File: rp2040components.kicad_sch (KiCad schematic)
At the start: 9 parts, among them J2 Conn_01x02, U8 W25Q128JVSIQTR, U9 ABM8-272-T3_C20625731

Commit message: Renamed page 2
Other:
- title: RP2040 basic -> RP2040 Components
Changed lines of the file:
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@@
 	(paper "A4")
 	(title_block
-		(title "RP2040 basic")
+		(title "RP2040 Components")
 	)
 	(text "Not sure if this is required. \nwe can optionally have a bootsel bridge \nhere. bridging QSPI_SS to GND\n-alister\n"

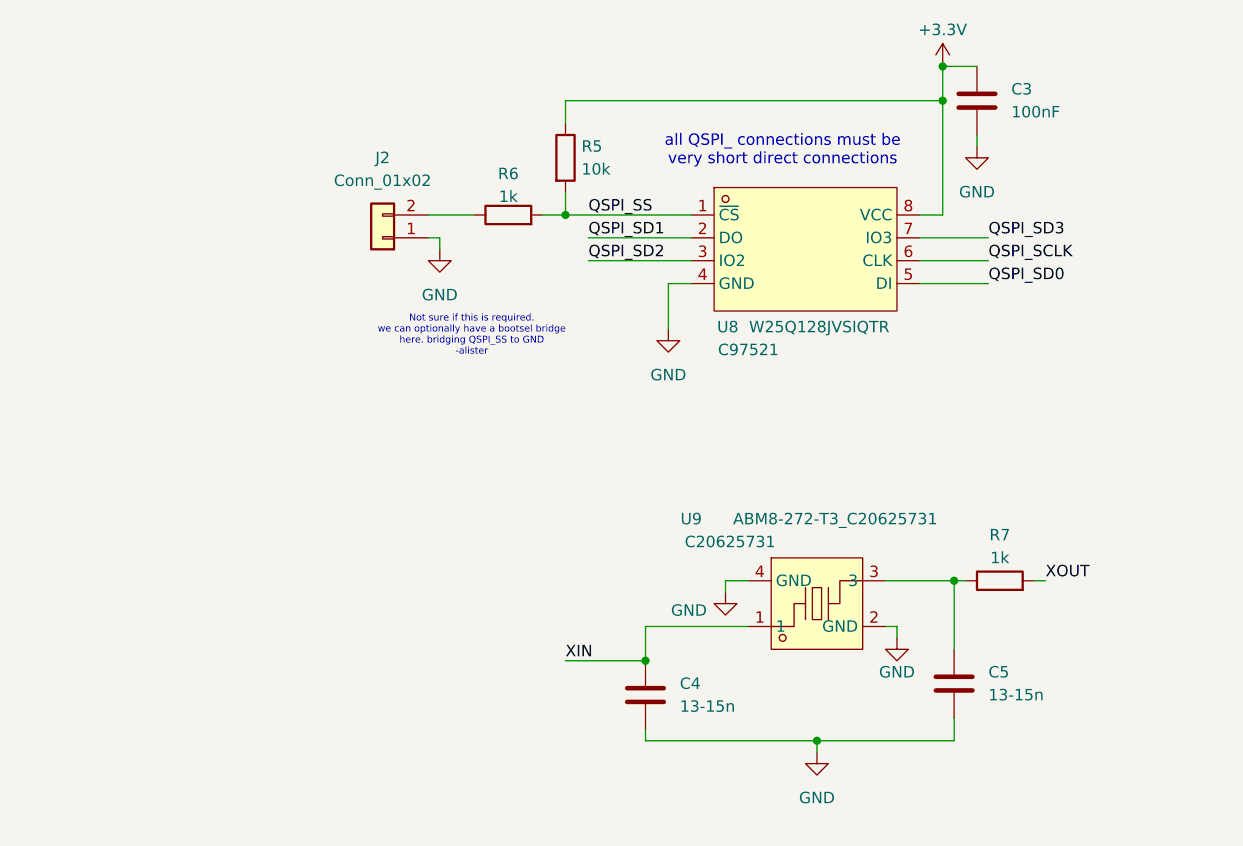
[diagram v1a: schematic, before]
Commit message: Add JLC part numbers, button and correct oscillator to Page 2
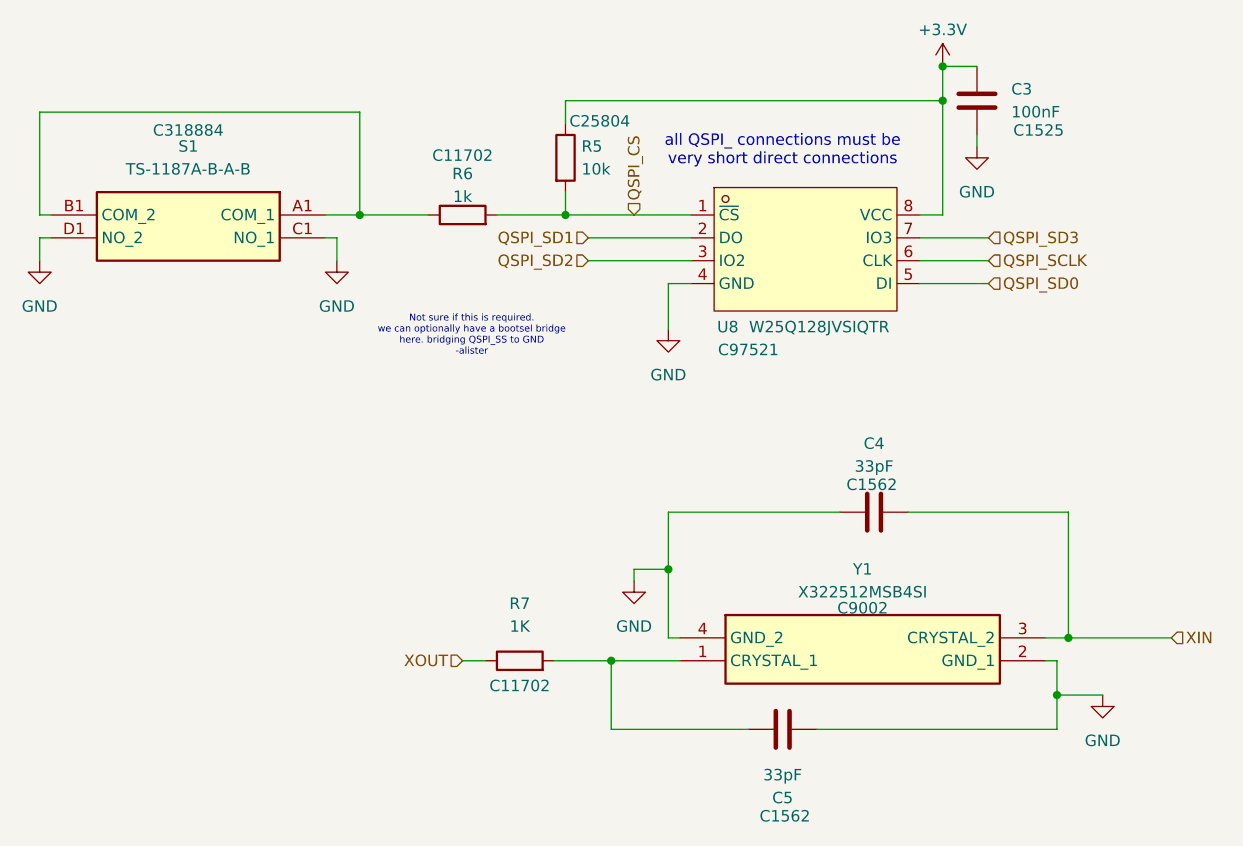
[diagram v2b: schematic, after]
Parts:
- removed J2: Conn_01x02, symbol Connector_Generic:Conn_01x02
- removed U9: ABM8-272-T3_C20625731, lcsc:CRYSTAL-SMD_4P-L3.2-W2.5-BL, symbol lcsc:ABM8-272-T3_C20625731
- added S1: TS-1187A-B-A-B, TS1187ABAB, symbol SamacSys_Parts:TS-1187A-B-A-B
- added Y1: X322512MSB4SI, X322512MSB4SI, symbol SamacSys_Parts:X322512MSB4SI
- C3: footprint (none) -> Capacitor_SMD:C_0402_1005Metric; LCSC PN (none) -> C1525
- C4, C5: value 13-15n -> 33pF; footprint (none) -> Capacitor_SMD:C_0402_1005Metric; LCSC PN (none) -> C1562
- R5: footprint (none) -> Resistor_SMD:R_0603_1608Metric; LCSC PN (none) -> C25804
- R6: footprint (none) -> Resistor_SMD:R_0402_1005Metric; LCSC PN (none) -> C11702
- R7: value 1k -> 1K; footprint (none) -> Resistor_SMD:R_0402_1005Metric; LCSC PN (none) -> C11702
- U8: LCSC PN (none) -> C97521; LCSC Part C97521 -> (none)
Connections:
- net GND: now also S1.C1 (NO_1), S1.D1 (NO_2), Y1.2 (GND_1), Y1.4 (GND_2)
- net XIN: now also Y1.3 (CRYSTAL_2)
- net XOUT: now also R7.1; no longer R7.2
- net at R6.1: now also S1.A1 (COM_1), S1.B1 (COM_2)
- net at C5.1: now also R7.2, Y1.1 (CRYSTAL_1); no longer R7.1
- net QSPI_SS renamed QSPI_CS
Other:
- moved on the sheet: R6

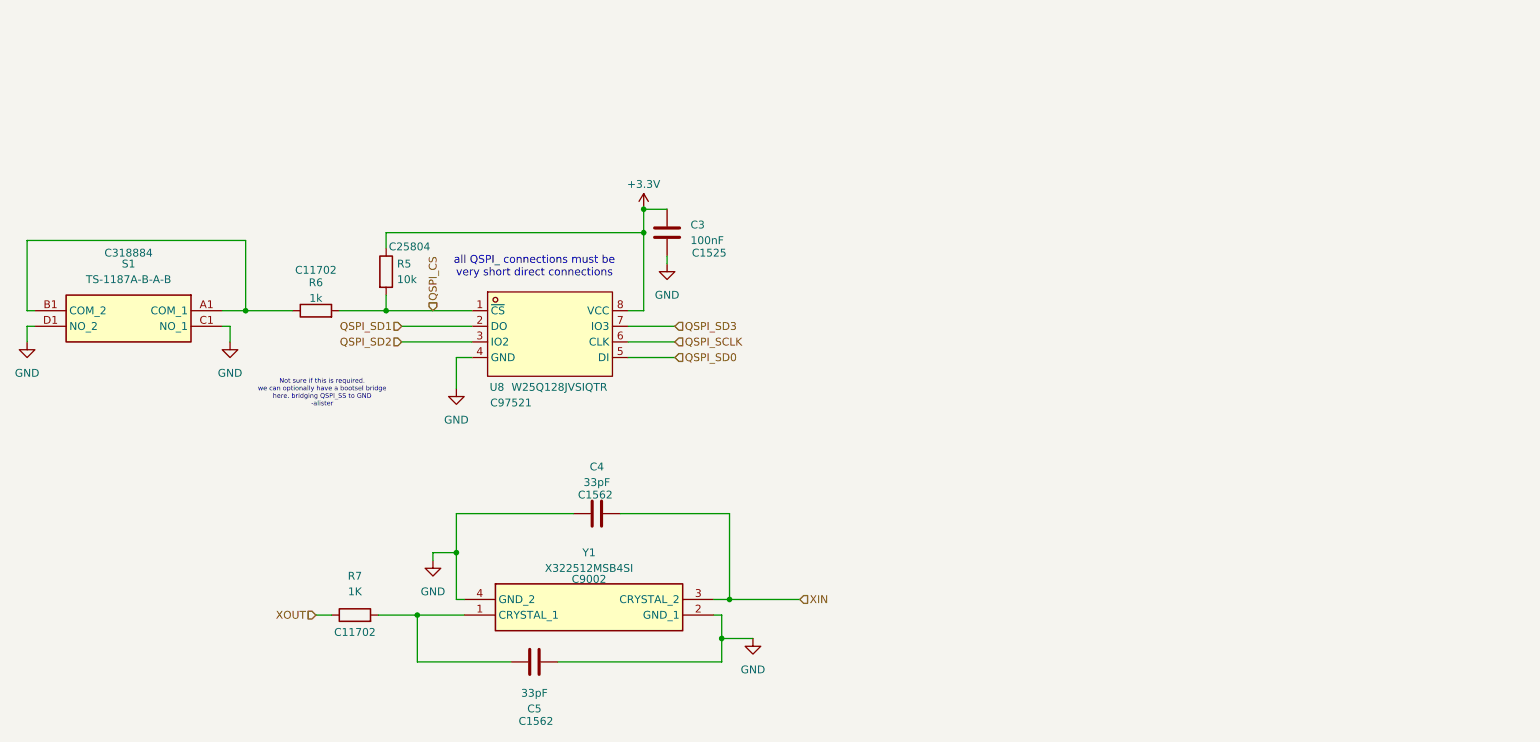
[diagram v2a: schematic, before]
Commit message: add temp sensor pull up fet and pull up resistor
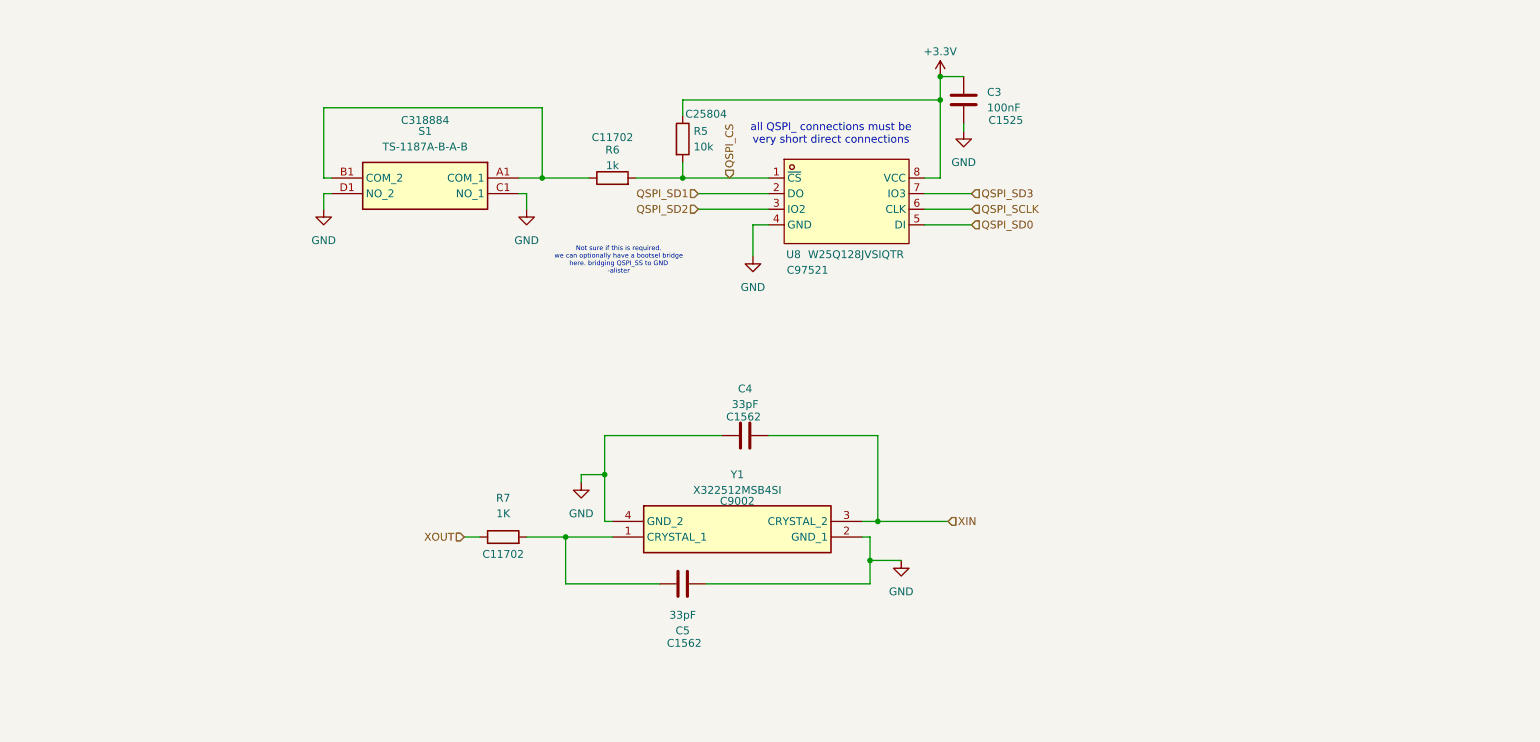
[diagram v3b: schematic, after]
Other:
- moved on the sheet: C3, C4, C5, R5, R6, R7, S1, U8, Y1

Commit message: add a whole bunch off stuff
- separated TFT display and HX711 into separate pages
- add ESD protection resistor to temp sensor
- corrected/added various JLC PCB part numbers
- swapped oscillator for the one used in part 1
- moved blocks of schematic around and into other pages to neaten it all up
- added file with download footprints, symbols, and 3D models
- add decoupling caps for RP2040
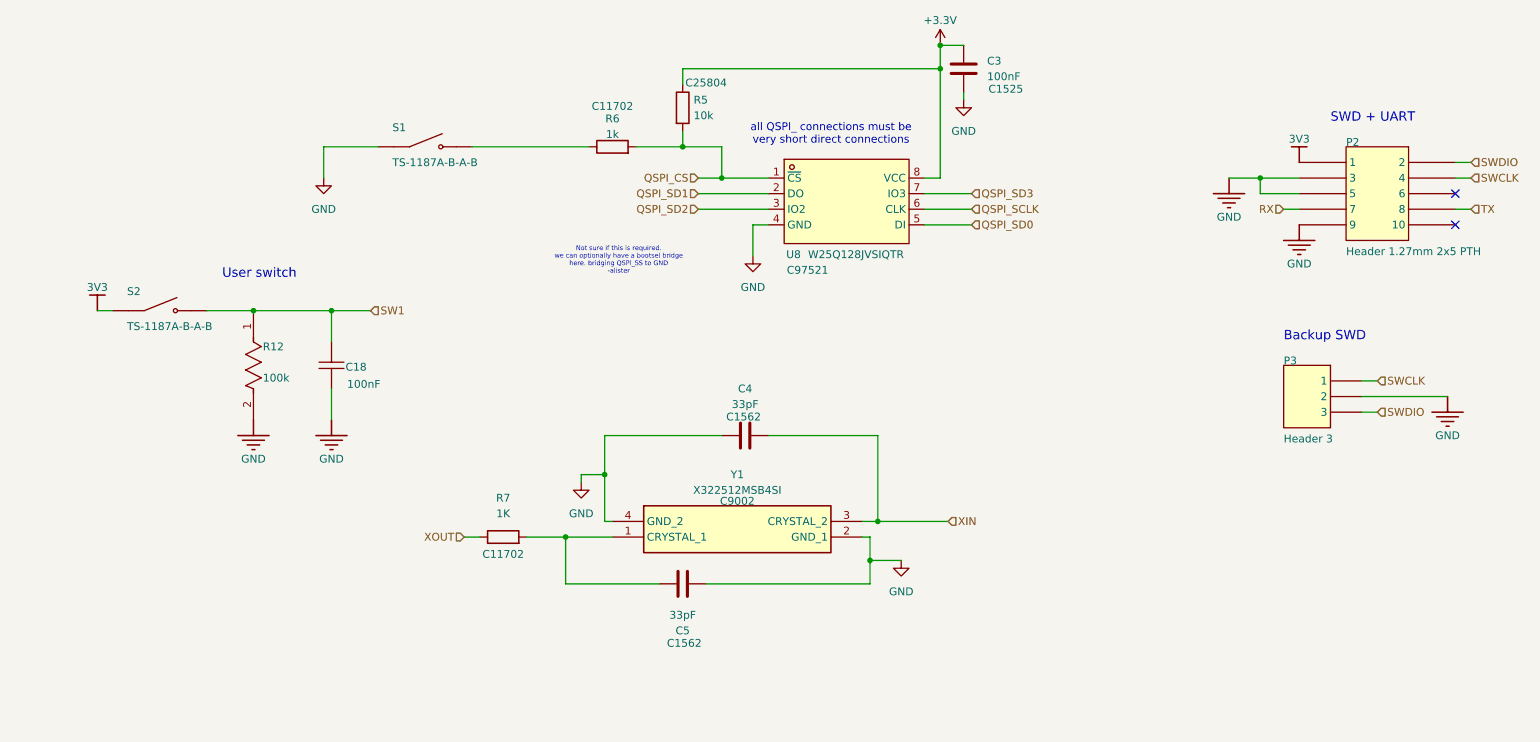
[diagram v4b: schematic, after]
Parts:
- removed S1: TS-1187A-B-A-B, TS1187ABAB, symbol SamacSys_Parts:TS-1187A-B-A-B
- added C18: CL05B104KO5NNNC, Imported Altium Library:CAPC1050X55X23ML05T13, symbol James Cook University:root_1_CAP-NP-2_James Cook University
- added P2: Header 1.27mm 2x5 PTH, Connector_PinHeader_1.27mm:PinHeader_2x05_P1.27mm_Vertical, symbol James Cook University:root_0_Header 1.27mm 2x5 PTH_James Cook University
- added P3: Header 3, Connector_PinHeader_2.54mm:PinHeader_1x03_P2.54mm_Vertical, symbol Miscellaneous Connectors:root_0_mirrored_Header 3_Miscellaneous Connectors.IntL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
- added R12: 0603WAF1003T5E, Imported Altium Library:FP-CRCW0603-e3-IPC_B, symbol James Cook University:root_3_1029c3af85768c4190bb7ad29bc67b5_James Cook Univers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
- added S1, S2: TS-1187A-B-A-B, Button_Switch_SMD:SW_Push_1P1T_XKB_TS-1187A, symbol James Cook University:root_0_TS-1187A-B-A-B_James Cook University
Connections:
- net GND: now also C18.1, P2.3, P2.5, P2.9, P3.2, R12.2, S1.A (COM), S1.B (COM)
- net at R6.1: now also S1.C (NO), S1.D (NO)
- new net 3V3: P2.1, S2.A (COM), S2.B (COM)
- new net RX: P2.7
- new net SW1: C18.2, R12.1, S2.C (NO), S2.D (NO)
- new net SWCLK: P2.4, P3.1
- new net SWDIO: P2.2, P3.3
- new net TX: P2.8
- no-connect marks 0 -> 2
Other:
- note added: "Backup SWD"
- note added: "SWD + UART"
- note added: "User switch"
- moved on the sheet: C3, R5, R6

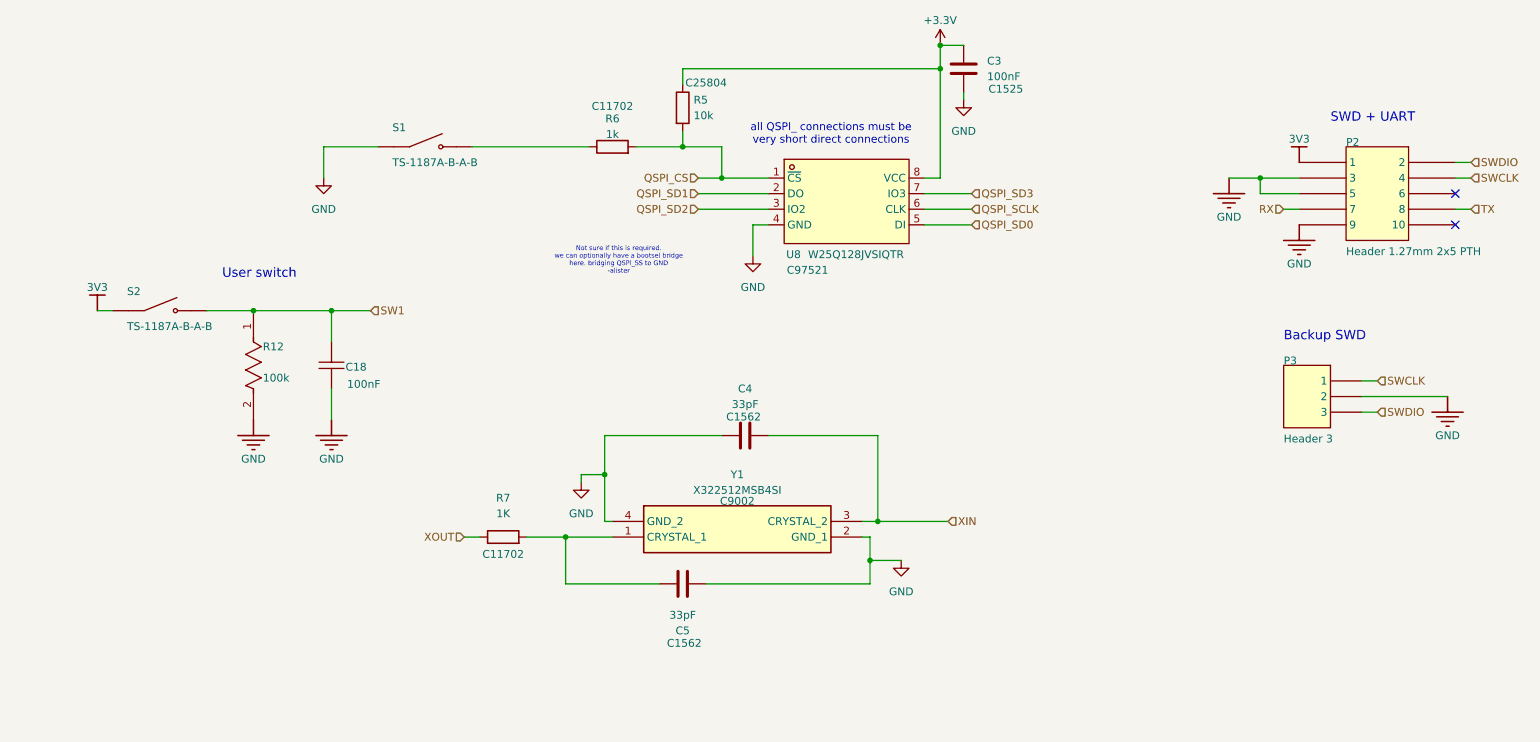
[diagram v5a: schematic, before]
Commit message: Breakout Board, ESD protection and TFT display updates
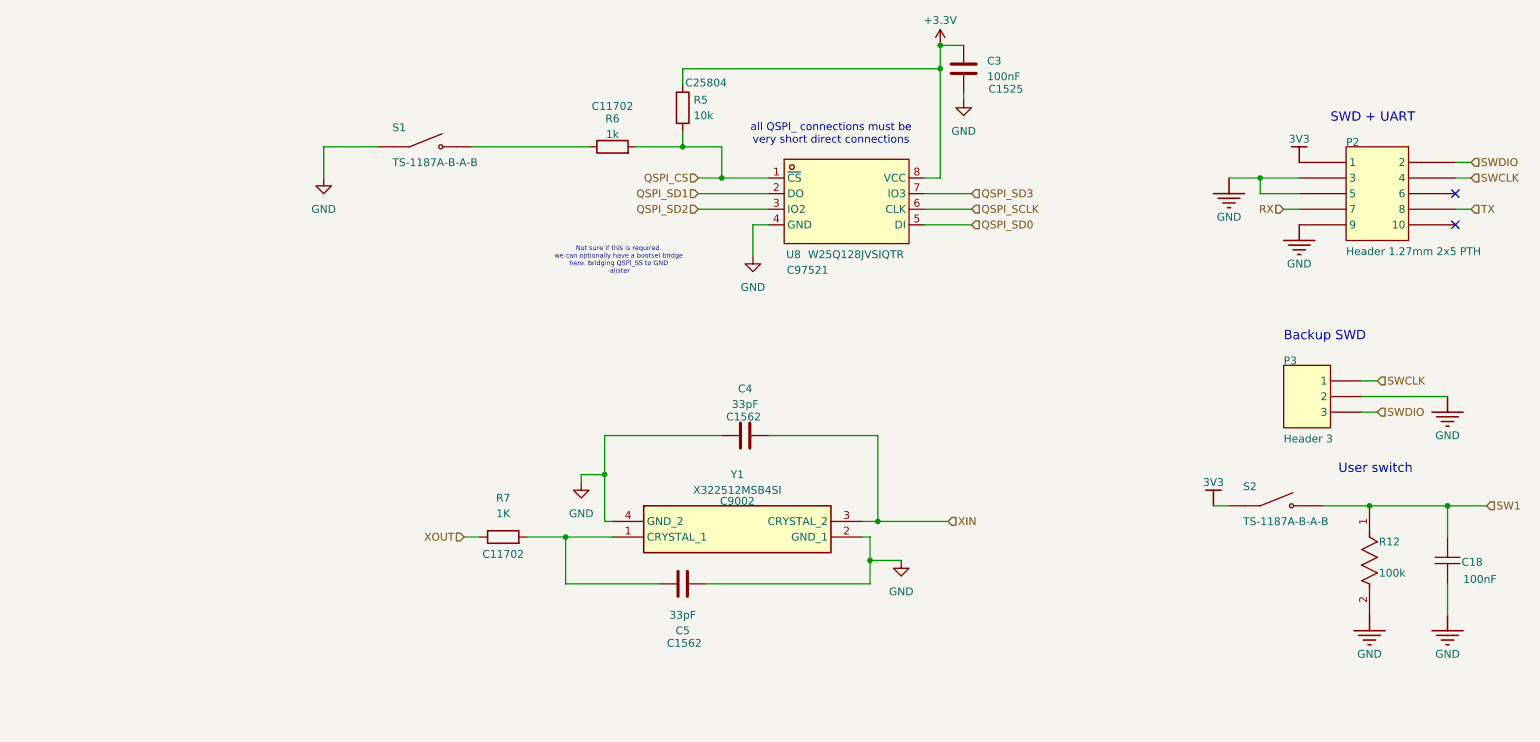
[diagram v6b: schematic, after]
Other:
- moved on the sheet: C18, R12, S2
